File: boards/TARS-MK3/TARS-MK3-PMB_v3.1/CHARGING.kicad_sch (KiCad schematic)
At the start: 0 parts

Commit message: test commit
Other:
- note added: "test commit"
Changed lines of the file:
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@@
     (rev "3.1")
   )
+  (text "test commit" (at 64.77 40.64 0)
+    (effects (font (size 1.27 1.27)) (justify left bottom))
+  )
 )

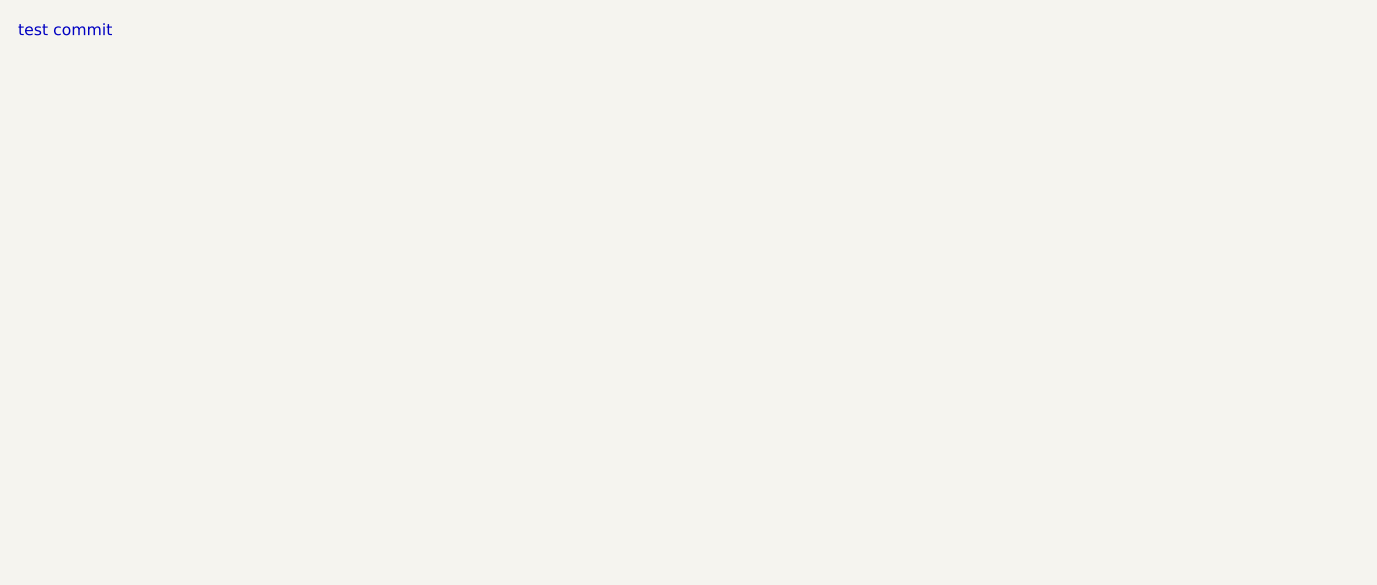
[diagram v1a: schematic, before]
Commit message: setup power schematic for future 3.1 dev
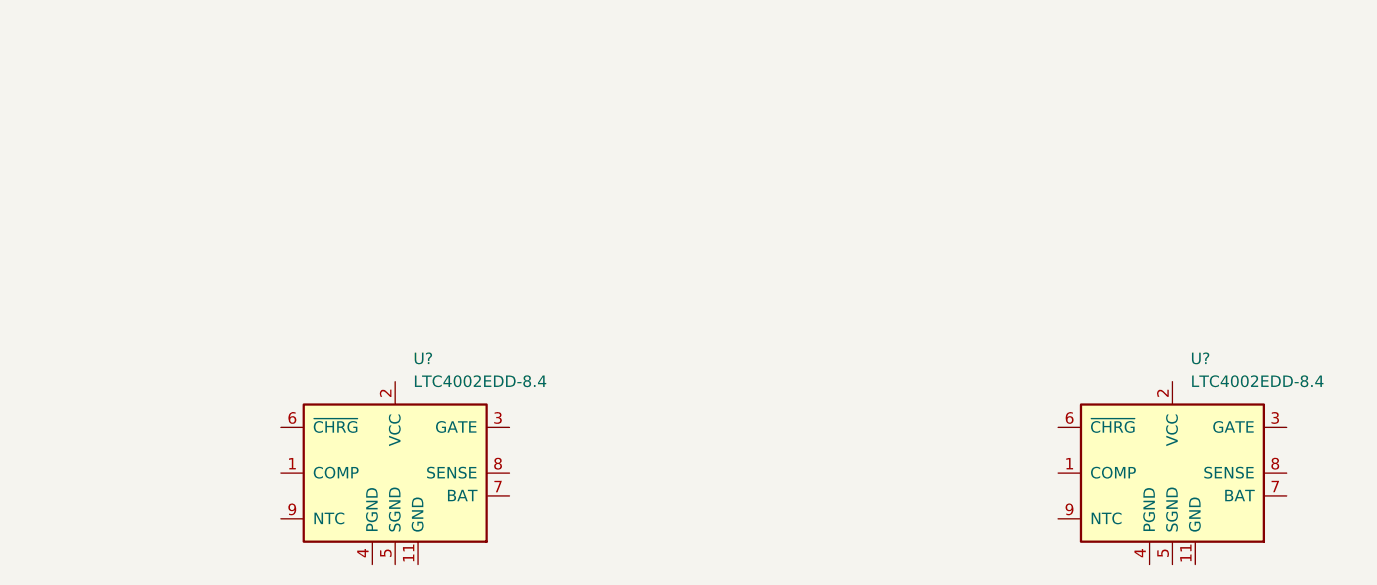
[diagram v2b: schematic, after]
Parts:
- added U? (x2): LTC4002EDD-8.4, Package_DFN_QFN:DFN-10-1EP_3x3mm_P0.5mm_EP1.55x2.48mm, symbol Battery_Management:LTC4002EDD-8.4
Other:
- note removed: "test commit"
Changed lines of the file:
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@@
     (rev "3.1")
   )
-  (text "test commit" (at 64.77 40.64 0)
-    (effects (font (size 1.27 1.27)) (justify left bottom))
+  (symbol (lib_id "Battery_Management:LTC4002EDD-8.4") (at 193.04 88.9 0) (unit 1)
+    (in_bom yes) (on_board yes) (fields_autoplaced)
+    (property "Reference" "U?" (id 0) (at 195.0594 76.2 0)
+      (effects (font (size 1.27 1.27)) (justify left))
+    )
+    (property "Value" "LTC4002EDD-8.4" (id 1) (at 195.0594 78.74 0)
+      (effects (font (size 1.27 1.27)) (justify left))
+    )
+    (property "Footprint" "Package_DFN_QFN:DFN-10-1EP_3x3mm_P0.5mm_EP1.55x2.48mm" (id 2) (at 193.04 100.33 0)
+      (effects (font (size 1.27 1.27)) hide)
+    )
+    (property "Datasheet" "https://www.analog.com/media/en/technical-documentation/data-sheets/4002f.pdf" (id 3) (at 182.88 80.01 0)
+      (effects (font (size 1.27 1.27)) hide)
+    )
+    (pin "1")
+    (pin "10")
+    (pin "11")
+    (pin "2")
+    (pin "3")
+    (pin "4")
+    (pin "5")
+    (pin "6")
+    (pin "7")
+    (pin "8")
+    (pin "9")
+  )
+  (symbol (lib_id "Battery_Management:LTC4002EDD-8.4") (at 106.68 88.9 0) (unit 1)
+    (in_bom yes) (on_board yes) (fields_autoplaced)
+    (property "Reference" "U?" (id 0) (at 108.6994 76.2 0)
+      (effects (font (size 1.27 1.27)) (justify left))
+    )
+    (property "Value" "LTC4002EDD-8.4" (id 1) (at 108.6994 78.74 0)
+      (effects (font (size 1.27 1.27)) (justify left))
+    )
+    (property "Footprint" "Package_DFN_QFN:DFN-10-1EP_3x3mm_P0.5mm_EP1.55x2.48mm" (id 2) (at 106.68 100.33 0)
+      (effects (font (size 1.27 1.27)) hide)
+    )
+    (property "Datasheet" "https://www.analog.com/media/en/technical-documentation/data-sheets/4002f.pdf" (id 3) (at 96.52 80.01 0)
+      (effects (font (size 1.27 1.27)) hide)
+    )
+    (pin "1")
+    (pin "10")
+    (pin "11")
+    (pin "2")
+    (pin "3")
+    (pin "4")
+    (pin "5")
+    (pin "6")
+    (pin "7")
+    (pin "8")
+    (pin "9")
   )
 )
